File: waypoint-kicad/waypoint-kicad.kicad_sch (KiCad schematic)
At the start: 83 parts, among them J1 USB_C_Receptacle_USB2.0_14P, J2 Conn_01x02, J3 Conn_Coaxial, J4 Conn_02x03_Odd_Even, J5 Conn_01x08, J6 Conn_01x02, Q1 NPN, SW1 SW_SPST, U1 nRF52840, U2 SX1262IMLTRT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

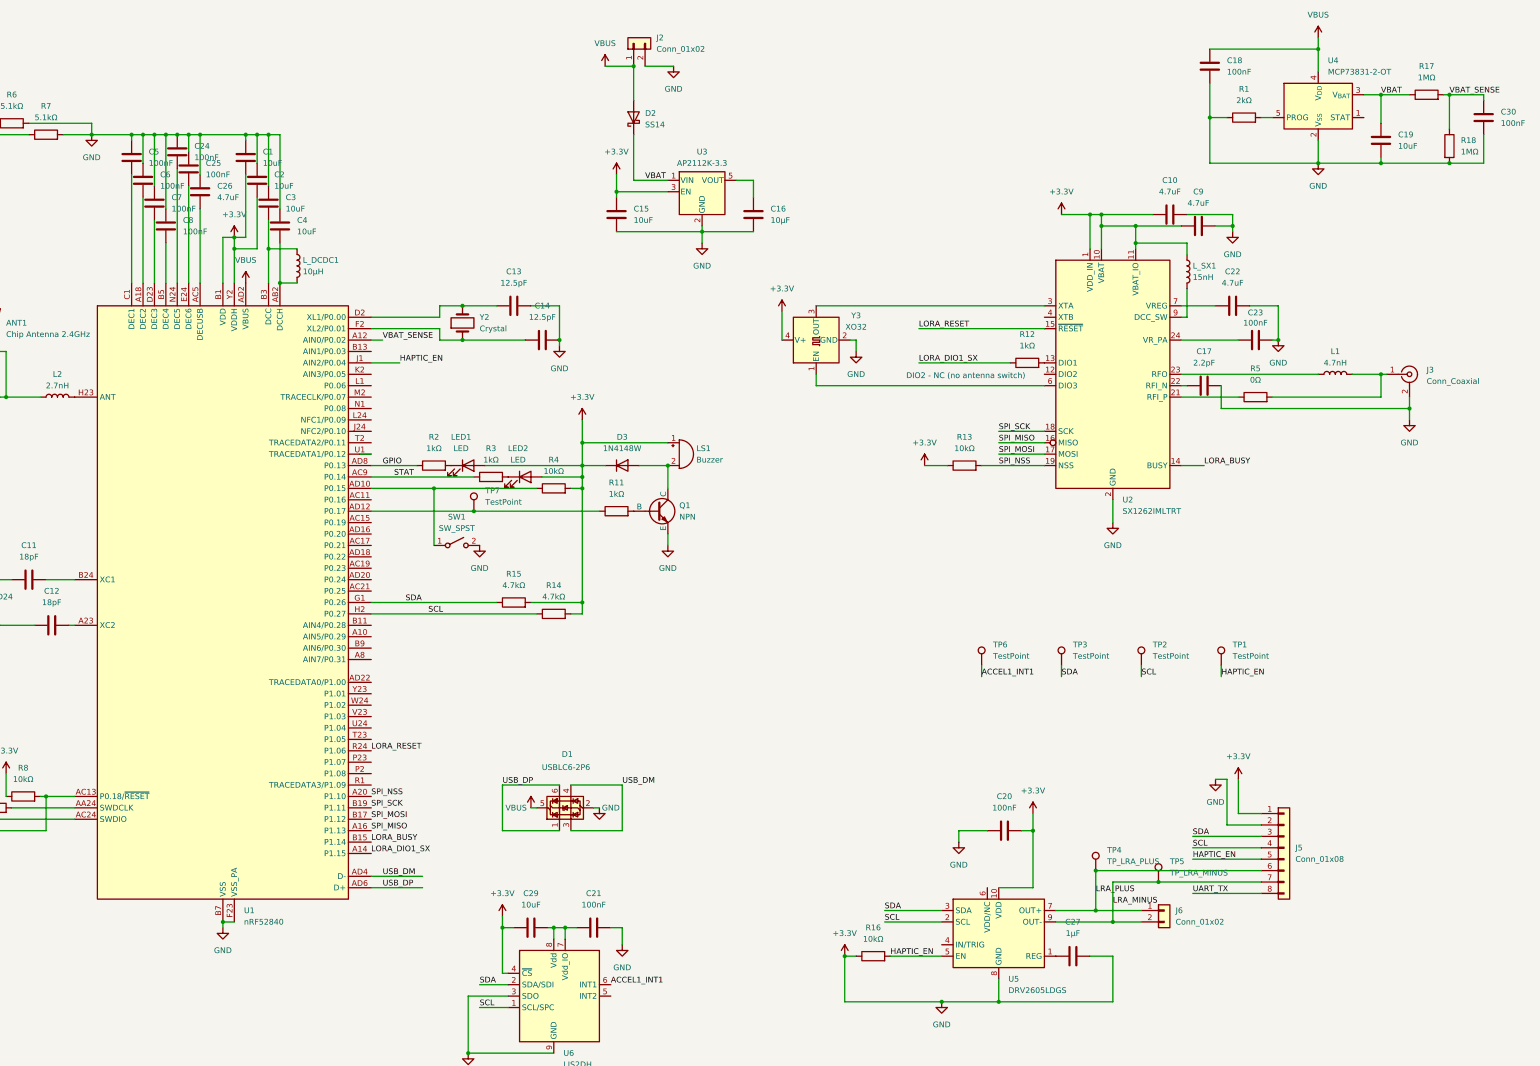
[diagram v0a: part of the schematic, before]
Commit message: Update project documentation and .gitignore
- Added a comprehensive datasheet collection for nRF52840 and SX1262, detailing critical design resources and specifications.
- Updated .gitignore to include 'exports' directory alongside 'freerouting.jar' to streamline file management.
- Removed outdated design changes comparison and review documents to enhance clarity and focus on current design specifications.
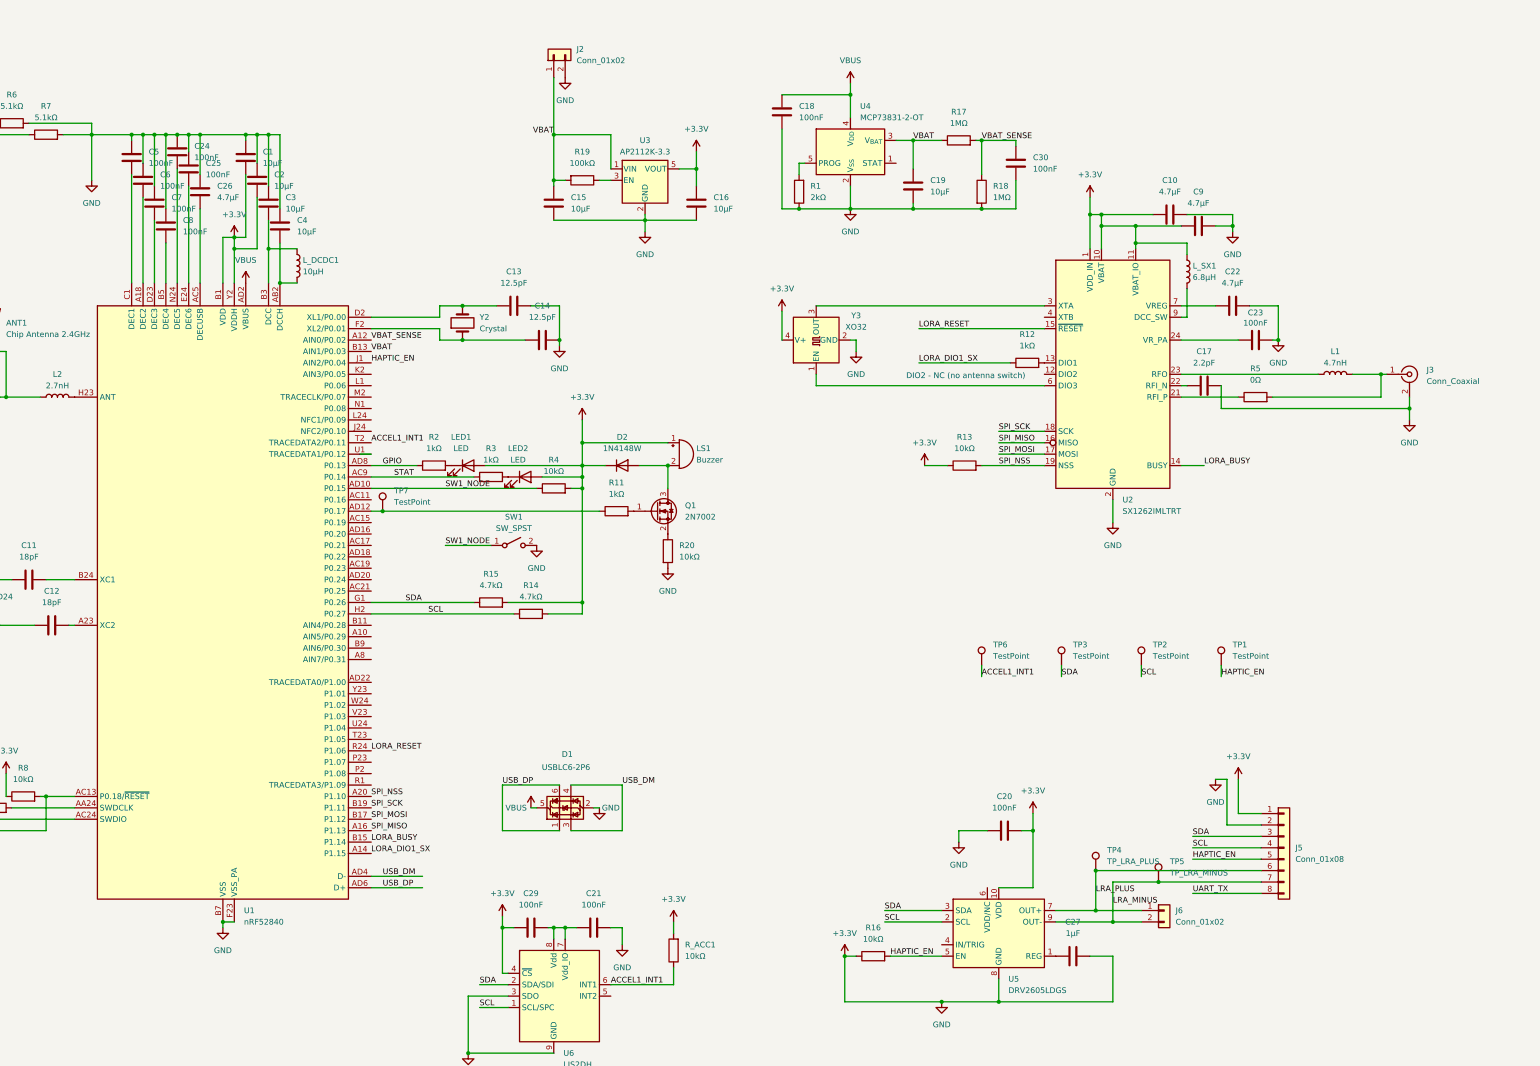
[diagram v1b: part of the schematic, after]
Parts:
- removed D2: SS14, Diode_SMD:D_SMA, symbol Diode:SS14
- removed Q1: NPN, Package_TO_SOT_SMD:SOT-23, symbol Simulation_SPICE:NPN
- added Q1: 2N7002, Package_TO_SOT_SMD:SOT-23, symbol Transistor_FET:2N7002
- added R19: 100kΩ, Resistor_SMD:R_0402_1005Metric_Pad0.72x0.64mm_HandSolder, symbol Device:R
- added R20, R_ACC1: 10kΩ, Resistor_SMD:R_0402_1005Metric_Pad0.72x0.64mm_HandSolder, symbol Device:R
- C1, C15, C19, C2, C3, C4: value 10uF -> 10µF
- C10, C22, C26, C9: value 4.7uF -> 4.7µF
- C29: value 10uF -> 100nF
- L_SX1: value 15nH -> 6.8µH
- renumbered D3 to D2
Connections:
- net +3.3V: now also C16.2, U3.5 (VOUT), R20.2, R_ACC1.2; no longer C15.2, U3.3 (EN)
- net ACCEL1_INT1: now also U1.T2 (TRACEDATA2/P0.11), R_ACC1.1
- net VBAT: now also C15.2, J2.1 (Pin_1), U1.B13 (AIN1/P0.03), R19.2
- net VBUS: no longer J2.1 (Pin_1)
- net SW1_NODE: now reaches R4.1, SW1.1 (A), U1.AD10 (P0.15)
- net at D2.2 (A), LS1.2 (-): now also Q1.3 (D)
- net at R11.2: now also Q1.1 (G)
- new net: Q1.2 (S), R20.1
- new net: R19.1, U3.3 (EN)
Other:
- moved on the sheet: C15, C16, C18, C19, C30, J2, R1, R14, R15, R17, R18, SW1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

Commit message: Add agent guidelines and datasheets for SX1262 and USB components
- Introduced AGENTS.md to outline project overview, key documents, and scripts for the Waypoint PCB design.
- Added datasheets for SX1261/SX1262, USB4105-GF-A, and USBLC6-2P6, summarizing key specifications and features.
- Updated waypoint-v2-design.md with component naming conventions and design verification processes.
- Implemented scripts for schematic verification and parsing, enhancing design review capabilities.
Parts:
- removed R_ACC1: 10kΩ, Resistor_SMD:R_0402_1005Metric_Pad0.72x0.64mm_HandSolder, symbol Device:R
- added C31: 100nF, Capacitor_SMD:C_0402_1005Metric_Pad0.74x0.62mm_HandSolder, symbol Device:C
- added R21: 10kΩ, Resistor_SMD:R_0402_1005Metric_Pad0.72x0.64mm_HandSolder, symbol Device:R
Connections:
- net +3.3V: now also Q1.2 (S), SW1.1 (A), C31.2, R21.2; no longer SW1.2 (B)
- net ACCEL1_INT1: now also R21.1
- net SW1_NODE: now also SW1.2 (B), C31.1; no longer SW1.1 (A)
- net at Q1.1 (G), R11.2: now also R20.1
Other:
- moved on the sheet: R11, R14, R15, R20, R4, SW1, TP7
